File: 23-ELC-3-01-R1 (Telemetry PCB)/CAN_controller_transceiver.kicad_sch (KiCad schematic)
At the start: 19 parts, among them U4 MCP2515-xSO, U5 SN65HVD230, Y1 16 MHz

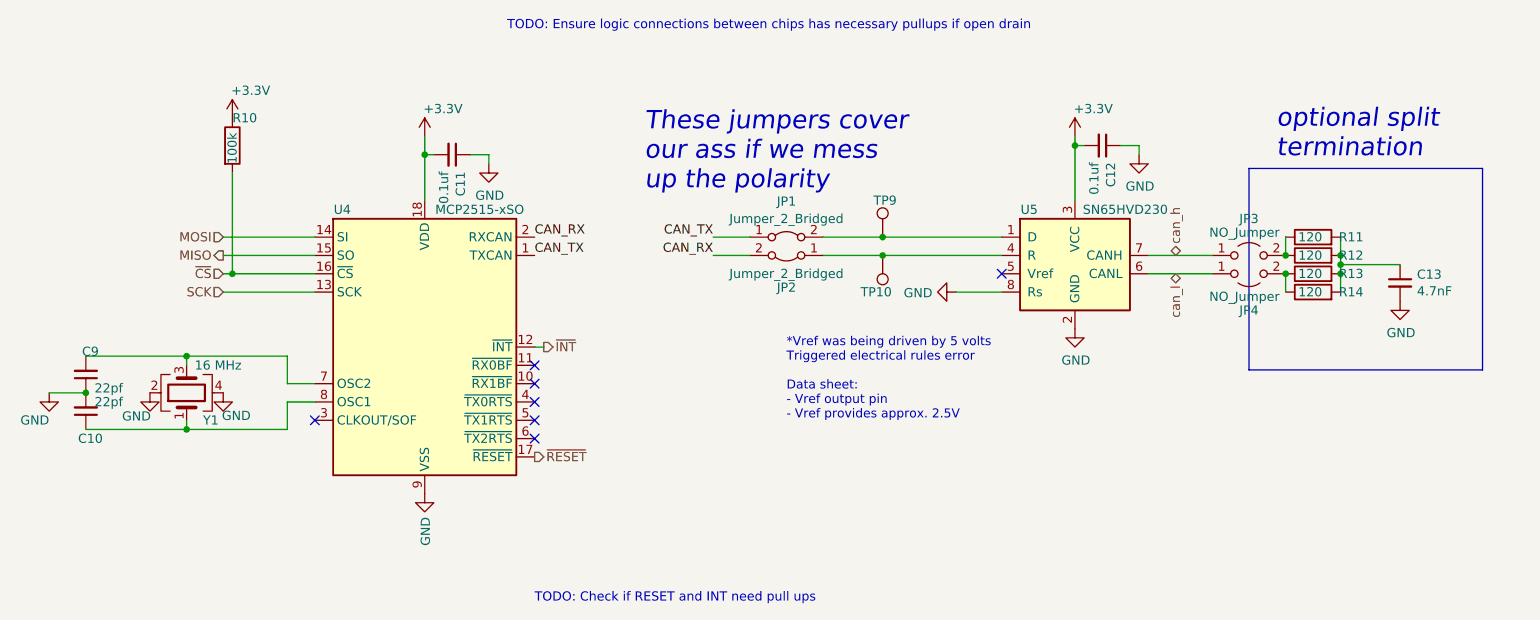
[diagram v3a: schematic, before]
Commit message: Changes for reference legibility, trace clearance, and through hole solder mask
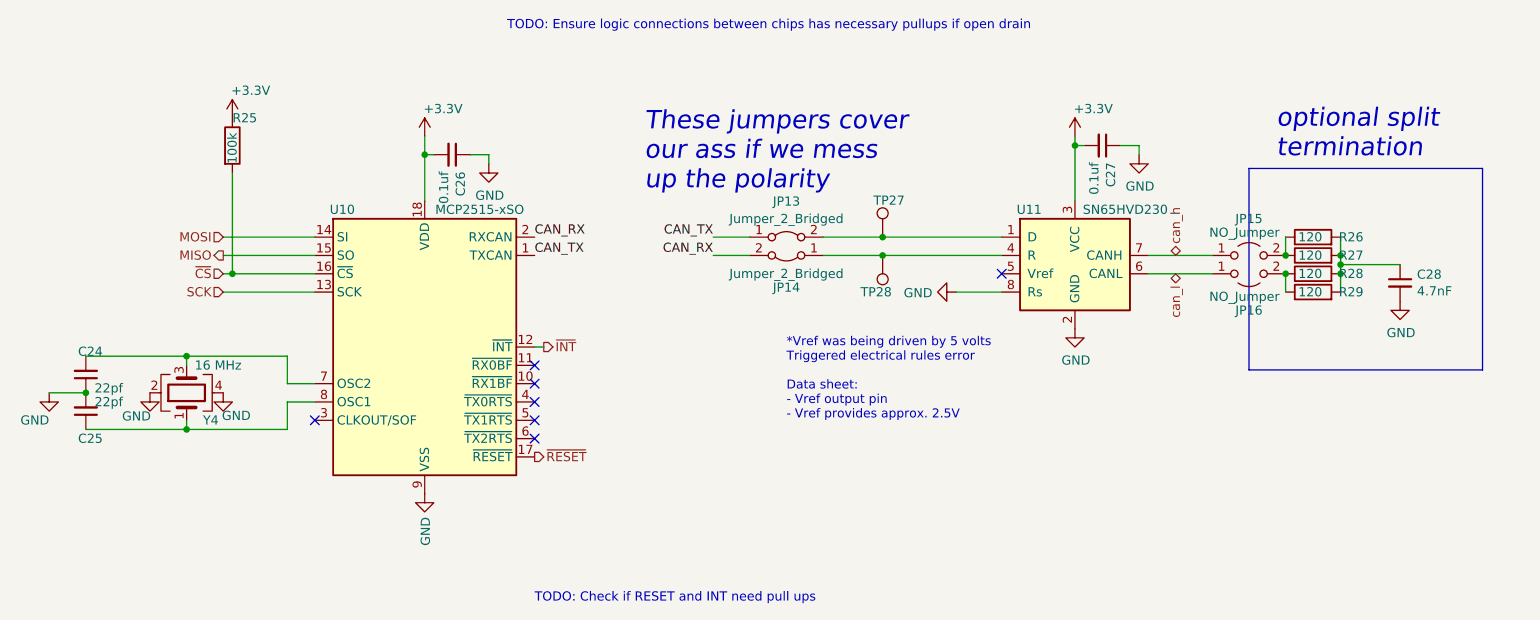
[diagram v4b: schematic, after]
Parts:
- renumbered C9 to C24, C10 to C25, C11 to C26, C12 to C27, C13 to C28, JP1 to JP13, JP2 to JP14, JP3 to JP15, JP4 to JP16, R10 to R25, R11 to R26, R12 to R27, R13 to R28, R14 to R29, TP9 to TP27, TP10 to TP28, U4 to U10, U5 to U11, Y1 to Y4
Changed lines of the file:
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@@
   (symbol (lib_id "Device:C_Small") (at 177.8 91.44 270)
     (in_bom yes) (on_board yes)
-    (property "Reference" "C12" (id 0) (at 178.9684 93.7768 0)
+    (property "Reference" "C27" (id 0) (at 178.9684 93.7768 0)
       (effects (font (size 1.27 1.27)) (justify left))
     )
@@
   (symbol (lib_id "power:GND") (at 173.99 116.84 0)
     (in_bom yes) (on_board yes)
-    (property "Reference" "#PWR051" (id 0) (at 173.99 123.19 0)
+    (property "Reference" "#PWR087" (id 0) (at 173.99 123.19 0)
       (effects (font (size 1.27 1.27)) hide)
     )
@@
   (symbol (lib_id "power:GND") (at 182.88 92.71 0)
     (in_bom yes) (on_board yes)
-    (property "Reference" "#PWR052" (id 0) (at 182.88 99.06 0)
+    (property "Reference" "#PWR088" (id 0) (at 182.88 99.06 0)
       (effects (font (size 1.27 1.27)) hide)
     )
@@
   (symbol (lib_id "power:GND") (at 157.48 111.76 270)
     (in_bom yes) (on_board yes)
-    (property "Reference" "#PWR049" (id 0) (at 151.13 111.76 0)
+    (property "Reference" "#PWR085" (id 0) (at 151.13 111.76 0)
       (effects (font (size 1.27 1.27)) hide)
     )
@@
   (symbol (lib_id "Interface_CAN_LIN:MCP2515-xSO") (at 83.82 119.38 0)
     (in_bom yes) (on_board yes)
-    (property "Reference" "U4" (id 0) (at 72.39 100.33 0))
+    (property "Reference" "U10" (id 0) (at 72.39 100.33 0))
     (property "Value" "MCP2515-xSO" (id 1) (at 91.44 100.33 0))
     (property "Footprint" "Package_SO:SOIC-18W_7.5x11.6mm_P1.27mm" (id 2) (at 83.82 142.24 0)
@@
   (symbol (lib_id "Interface_CAN_LIN:SN65HVD230") (at 173.99 106.68 0)
     (in_bom yes) (on_board yes)
-    (property "Reference" "U5" (id 0) (at 167.64 100.33 0))
+    (property "Reference" "U11" (id 0) (at 167.64 100.33 0))
     (property "Value" "SN65HVD230" (id 1) (at 180.975 100.33 0))
     (property "Footprint" "Package_SO:SOIC-8_3.9x4.9mm_P1.27mm" (id 2) (at 173.99 119.38 0)
@@
   (symbol (lib_id "Device:Crystal_GND24") (at 50.8 125.73 90)
     (in_bom yes) (on_board yes)
-    (property "Reference" "Y1" (id 0) (at 55.245 129.54 90)
+    (property "Reference" "Y4" (id 0) (at 55.245 129.54 90)
       (effects (font (size 1.27 1.27)) (justify left))
     )
@@
   (symbol (lib_id "power:GND") (at 83.82 139.7 0)
     (in_bom yes) (on_board yes)
-    (property "Reference" "#PWR047" (id 0) (at 83.82 146.05 0)
+    (property "Reference" "#PWR083" (id 0) (at 83.82 146.05 0)
       (effects (font (size 1.27 1.27)) hide)
     )
@@
   (symbol (lib_id "power:GND") (at 45.72 125.73 0)
     (in_bom yes) (on_board yes)
-    (property "Reference" "#PWR043" (id 0) (at 45.72 132.08 0)
+    (property "Reference" "#PWR079" (id 0) (at 45.72 132.08 0)
       (effects (font (size 1.27 1.27)) hide)
     )
@@
   (symbol (lib_id "power:GND") (at 55.88 125.73 0)
     (in_bom yes) (on_board yes)
-    (property "Reference" "#PWR044" (id 0) (at 55.88 132.08 0)
+    (property "Reference" "#PWR080" (id 0) (at 55.88 132.08 0)
       (effects (font (size 1.27 1.27)) hide)
     )
@@
   (symbol (lib_id "Device:C_Small") (at 36.83 123.19 180)
     (in_bom yes) (on_board yes)
-    (property "Reference" "C9" (id 0) (at 37.465 120.015 0))
+    (property "Reference" "C24" (id 0) (at 37.465 120.015 0))
     (property "Value" "22pf" (id 1) (at 40.005 125.095 0))
     (property "Footprint" "Capacitor_SMD:C_0603_1608Metric_Pad1.08x0.95mm_HandSolder" (id 2) (at 36.83 123.19 0)
@@
   (symbol (lib_id "Device:C_Small") (at 36.83 128.27 180)
     (in_bom yes) (on_board yes)
-    (property "Reference" "C10" (id 0) (at 37.465 132.08 0))
+    (property "Reference" "C25" (id 0) (at 37.465 132.08 0))
     (property "Value" "22pf" (id 1) (at 40.005 127 0))
     (property "Footprint" "Capacitor_SMD:C_0603_1608Metric_Pad1.08x0.95mm_HandSolder" (id 2) (at 36.83 128.27 0)
@@
   (symbol (lib_id "power:GND") (at 31.75 125.73 0)
     (in_bom yes) (on_board yes)
-    (property "Reference" "#PWR042" (id 0) (at 31.75 132.08 0)
+    (property "Reference" "#PWR078" (id 0) (at 31.75 132.08 0)
       (effects (font (size 1.27 1.27)) hide)
     )
@@
   (symbol (lib_id "Device:C_Small") (at 87.63 92.71 270)
     (in_bom yes) (on_board yes)
-    (property "Reference" "C11" (id 0) (at 88.7984 95.0468 0)
+    (property "Reference" "C26" (id 0) (at 88.7984 95.0468 0)
       (effects (font (size 1.27 1.27)) (justify left))
     )
@@
   (symbol (lib_id "power:GND") (at 92.71 93.98 0)
     (in_bom yes) (on_board yes)
-    (property "Reference" "#PWR048" (id 0) (at 92.71 100.33 0)
+    (property "Reference" "#PWR084" (id 0) (at 92.71 100.33 0)
       (effects (font (size 1.27 1.27)) hide)
     )
@@
   (symbol (lib_id "Device:R") (at 57.15 91.44 0)
     (in_bom yes) (on_board yes)
-    (property "Reference" "R10" (id 0) (at 57.15 87.63 0)
+    (property "Reference" "R25" (id 0) (at 57.15 87.63 0)
       (effects (font (size 1.27 1.27)) (justify left))
     )
@@
   (symbol (lib_id "Connector:TestPoint") (at 147.32 104.14 0)
     (in_bom yes) (on_board yes)
-    (property "Reference" "TP9" (id 0) (at 146.05 99.06 0)
+    (property "Reference" "TP27" (id 0) (at 146.05 99.06 0)
       (effects (font (size 1.27 1.27)) (justify left))
     )
@@
   (symbol (lib_id "Connector:TestPoint") (at 147.32 106.68 180)
     (in_bom yes) (on_board yes)
-    (property "Reference" "TP10" (id 0) (at 148.59 111.76 0)
+    (property "Reference" "TP28" (id 0) (at 148.59 111.76 0)
       (effects (font (size 1.27 1.27)) (justify left))
     )
@@
   (symbol (lib_id "Jumper:Jumper_2_Bridged") (at 133.985 104.14 0)
     (in_bom yes) (on_board yes)
-    (property "Reference" "JP1" (id 0) (at 133.985 99.187 0))
+    (property "Reference" "JP13" (id 0) (at 133.985 99.187 0))
     (property "Value" "Jumper_2_Bridged" (id 1) (at 133.985 101.6 0))
     (property "Footprint" "Jumper:SolderJumper-2_P1.3mm_Bridged_RoundedPad1.0x1.5mm" (id 2) (at 133.985 104.14 0)
@@
   (symbol (lib_id "Jumper:Jumper_2_Bridged") (at 133.985 106.68 180)
     (in_bom yes) (on_board yes)
-    (property "Reference" "JP2" (id 0) (at 133.985 111.125 0))
+    (property "Reference" "JP14" (id 0) (at 133.985 111.125 0))
     (property "Value" "Jumper_2_Bridged" (id 1) (at 133.985 109.22 0))
     (property "Footprint" "Jumper:SolderJumper-2_P1.3mm_Bridged_RoundedPad1.0x1.5mm" (id 2) (at 133.985 106.68 0)
@@
   (symbol (lib_id "Jumper:Jumper_2_Open") (at 198.12 106.68 0)
     (in_bom yes) (on_board yes)
-    (property "Reference" "JP3" (id 0) (at 198.12 101.6 0))
+    (property "Reference" "JP15" (id 0) (at 198.12 101.6 0))
     (property "Value" "NO_Jumper" (id 1) (at 197.485 103.505 0))
     (property "Footprint" "Jumper:SolderJumper-2_P1.3mm_Open_RoundedPad1.0x1.5mm" (id 2) (at 198.12 106.68 0)
@@
   (symbol (lib_id "Jumper:Jumper_2_Open") (at 198.12 109.22 0) (mirror x)
     (in_bom yes) (on_board yes)
-    (property "Reference" "JP4" (id 0) (at 198.12 114.3 0))
+    (property "Reference" "JP16" (id 0) (at 198.12 114.3 0))
     (property "Value" "NO_Jumper" (id 1) (at 197.485 112.395 0))
     (property "Footprint" "Jumper:SolderJumper-2_P1.3mm_Open_RoundedPad1.0x1.5mm" (id 2) (at 198.12 109.22 0)
@@
   (symbol (lib_id "Device:C_Small") (at 219.075 110.49 0)
     (in_bom yes) (on_board yes)
-    (property "Reference" "C13" (id 0) (at 221.4118 109.3216 0)
+    (property "Reference" "C28" (id 0) (at 221.4118 109.3216 0)
       (effects (font (size 1.27 1.27)) (justify left))
     )
@@
   (symbol (lib_id "Device:R") (at 207.01 106.68 90)
     (in_bom yes) (on_board yes)
-    (property "Reference" "R12" (id 0) (at 213.995 106.68 90)
+    (property "Reference" "R27" (id 0) (at 213.995 106.68 90)
       (effects (font (size 1.27 1.27)) (justify left))
     )
@@
   (symbol (lib_id "Device:R") (at 207.01 104.14 90)
     (in_bom yes) (on_board yes)
-    (property "Reference" "R11" (id 0) (at 213.995 104.14 90)
+    (property "Reference" "R26" (id 0) (at 213.995 104.14 90)
       (effects (font (size 1.27 1.27)) (justify left))
     )
@@
   (symbol (lib_id "Device:R") (at 207.01 109.22 90)
     (in_bom yes) (on_board yes)
-    (property "Reference" "R13" (id 0) (at 213.995 109.22 90)
+    (property "Reference" "R28" (id 0) (at 213.995 109.22 90)
       (effects (font (size 1.27 1.27)) (justify left))
     )
@@
   (symbol (lib_id "Device:R") (at 207.01 111.76 90)
     (in_bom yes) (on_board yes)
-    (property "Reference" "R14" (id 0) (at 213.995 111.76 90)
+    (property "Reference" "R29" (id 0) (at 213.995 111.76 90)
       (effects (font (size 1.27 1.27)) (justify left))
     )
@@
   (symbol (lib_id "power:GND") (at 219.075 113.03 0)
     (in_bom yes) (on_board yes)
-    (property "Reference" "#PWR053" (id 0) (at 219.075 119.38 0)
+    (property "Reference" "#PWR089" (id 0) (at 219.075 119.38 0)
       (effects (font (size 1.27 1.27)) hide)
     )
@@
   (symbol (lib_id "power:+3.3V") (at 57.15 87.63 0)
     (in_bom yes) (on_board yes)
-    (property "Reference" "#PWR045" (id 0) (at 57.15 91.44 0)
+    (property "Reference" "#PWR081" (id 0) (at 57.15 91.44 0)
       (effects (font (size 1.27 1.27)) hide)
     )
@@
   (symbol (lib_id "power:+3.3V") (at 83.82 90.17 0)
     (in_bom yes) (on_board yes)
-    (property "Reference" "#PWR046" (id 0) (at 83.82 93.98 0)
+    (property "Reference" "#PWR082" (id 0) (at 83.82 93.98 0)
       (effects (font (size 1.27 1.27)) hide)
     )
@@
   (symbol (lib_id "power:+3.3V") (at 173.99 90.17 0)
     (in_bom yes) (on_board yes)
-    (property "Reference" "#PWR050" (id 0) (at 173.99 93.98 0)
-      (effects (font (size 1.27 1.27)) hide)
-    )
+    (property "Reference" "#PWR086" (id 0) (at 173.99 93.98 0)
+      (effects (font (size 1.27 1.27)) hide)
+    )
